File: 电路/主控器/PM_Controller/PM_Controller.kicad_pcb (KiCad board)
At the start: 4 copper layers, 47.5 x 92.5 mm, 117 parts, among them J1 Conn_01x04_Pin, Q1 FDV301N, Q2 FDV301N, Q3 SS8550, SW1 TS-1088R-02026, SW2 TS-1088R-02026, SW3 TS-1088R-02026, SW4 TS-1088R-02026, SW5 TS-1088R-02026, U1 ESP32-S3-WROOM-1, U10 TPS7A0233PDBVR, U11 SN74AUP1G17DBVR, U12 24C64, U13 ZX-ZH1.5-3PWT, U14 TPS563201, U15 ZX-ZH1.5-4PWT, U16 TLP291, U18 TPS3808G01DBVR, U19 ZX-ZH1.5-5PWT, U2 TP4057, U3 SN74AUP1G74DCUR, U4 TPS563201, U5 DRV8251ADDAR, U6 74HC165, U7 USBLC6-2SC6, U8 ZX-XH2.54-5PWT, U9 ZX-ZH1.5-4PWT

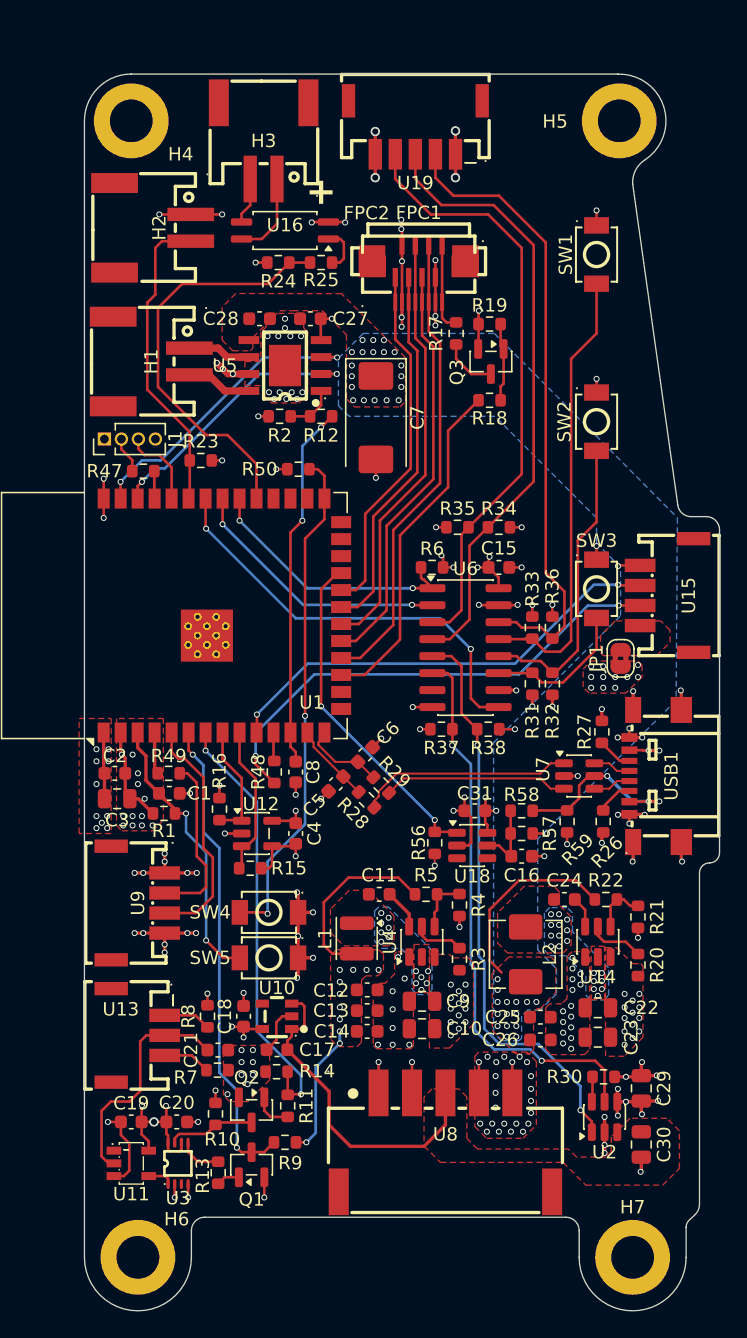
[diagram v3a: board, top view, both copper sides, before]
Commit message: 保存 PM_Controller Rev2.0 投产快照及 Rev3 装配更新
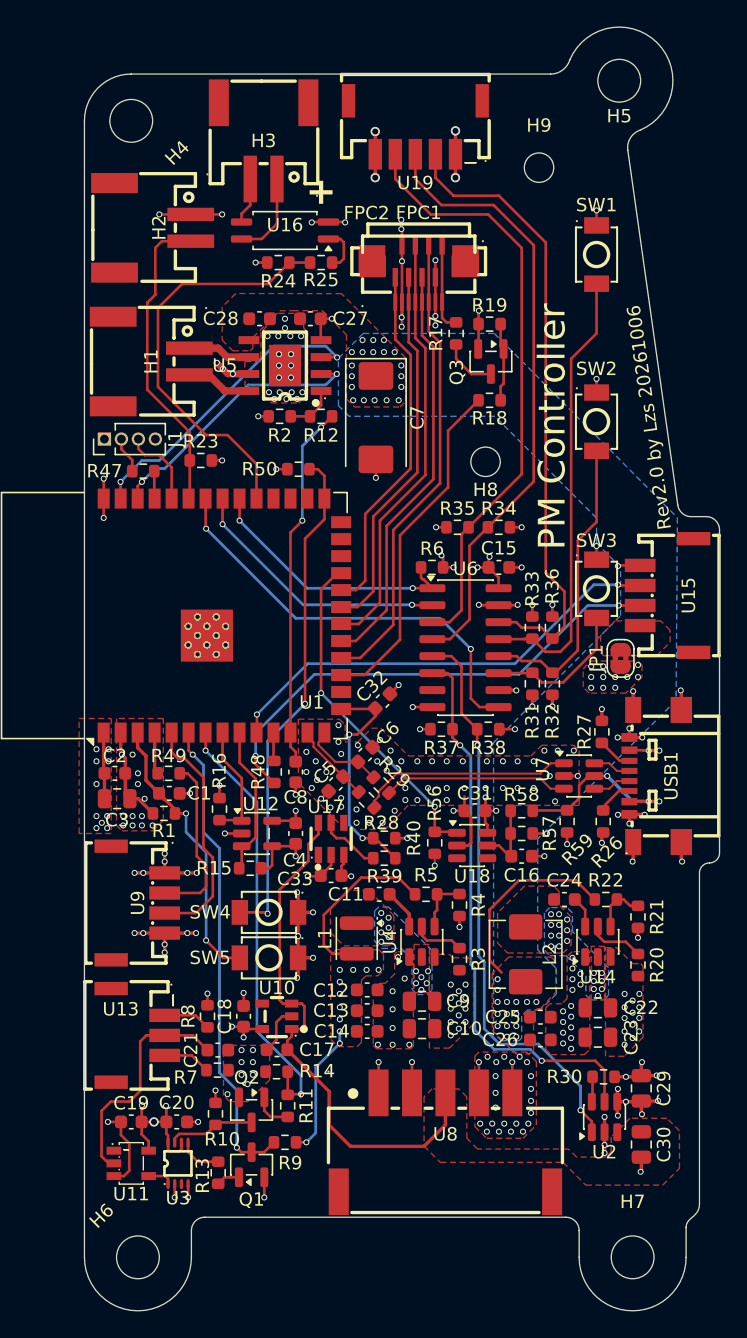
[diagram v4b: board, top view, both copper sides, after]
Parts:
- added C32: TBD(1uf), Capacitor_SMD:C_0603_1608Metric, F.Cu at (67.7, 136.4)
- added C33: 100nF, Capacitor_SMD:C_0603_1608Metric, F.Cu at (63.8, 149.4)
- added H8: MountingHole, MountingHole:MountingHole_2.2mm_M2, F.Cu at (75.4, 118.5)
- added H9: MountingHole, MountingHole:MountingHole_2.2mm_M2, F.Cu at (79.4, 96.5)
- added R39: 100k, Resistor_SMD:R_0603_1608Metric, F.Cu at (67.8, 148.2)
- added R40: 100k, Resistor_SMD:R_0603_1608Metric, F.Cu at (67.8, 146.7)
- added U17: TPG4599S6, EasyEDA:TSOT-23-6_L2.9-W1.6-P0.95-LS2.8-BL, F.Cu at (63.8, 146.7)
- H4, H5, H6, H7: footprint MountingHole:MountingHole_3.2mm_M3_DIN965_Pad -> MountingHole:MountingHole_3.2mm_M3
- moved H5 3.00 mm to (85.4, 90.0)
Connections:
- U1 pad 15: unconnected-(U1-IO3-Pad15) -> /ADC_BAT
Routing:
- net /ADC_BAT: track 0.00 -> 16.9 mm, vias 0 -> 2
- net +BATT: track 24.5 -> 40.0 mm
- net /ADC_BAT_BAT: track 0.00 -> 4.69 mm
- net GND: track 114.4 -> 118.4 mm, vias 153 -> 207
- net +3.3V: track 80.1 -> 84.1 mm, vias 57 -> 58
- net /MotorPWM_A: track 22.5 -> 23.2 mm
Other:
- board size 47.5 x 92.5 mm -> 47.5 x 96 mm
- board text added: "PM Controller"
- board text added: "Rev2.0 by Lzs 20261006"
